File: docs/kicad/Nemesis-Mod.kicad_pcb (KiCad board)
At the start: 2 copper layers, 45.7 x 59.7 mm, 6 parts, among them P1 Pololu_5V_Step_Down_Regulator, SW1 SW1

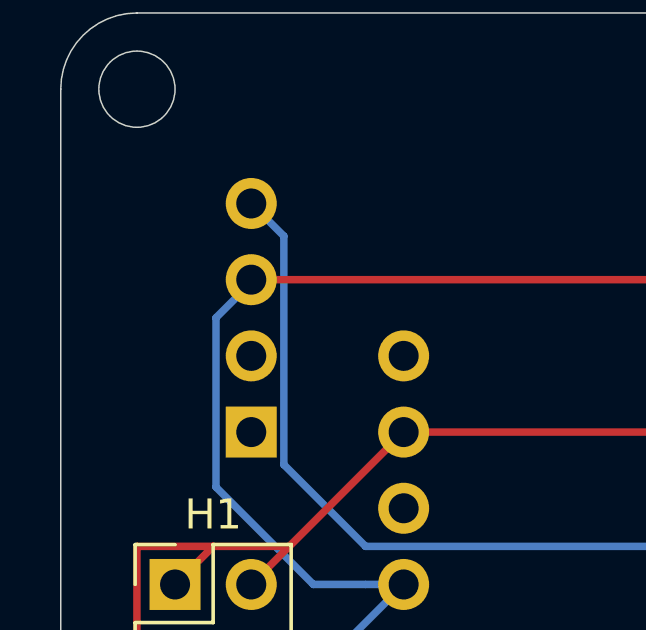
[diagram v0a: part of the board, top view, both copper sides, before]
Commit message: Adding on-board documentation for power.
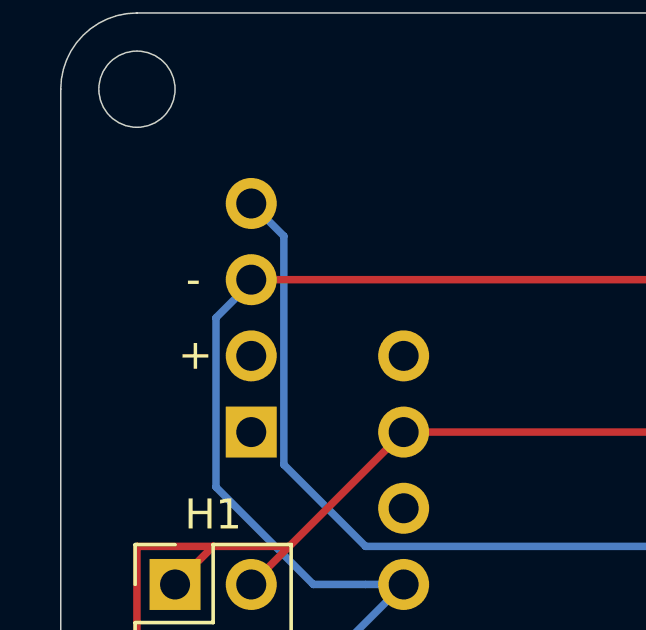
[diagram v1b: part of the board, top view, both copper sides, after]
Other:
- board text added: "+"
- board text added: "-"
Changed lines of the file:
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@@
     (property "Sheetname" "Mainboard")
     (attr through_hole)
-    (fp_text reference "P1" (at 0 -7.62 90) (layer "B.SilkS")
+    (fp_text reference "P1" (at 0 -7.0612 90) (layer "B.SilkS")
       (effects (font (size 1 1) (thickness 0.15)) (justify mirror))
     )
@@
   (gr_circle (center 132.08 80.01) (end 133.35 80.01) (layer "Edge.Cuts") (width 0.05) (fill none))
   (gr_line (start 134.62 80.01) (end 134.62 129.54) (layer "Edge.Cuts") (width 0.05))
+  (gr_text "-" (at 93.3196 86.36) (layer "F.SilkS")
+    (effects (font (size 1 1) (thickness 0.15)))
+  )
+  (gr_text "+" (at 93.4212 88.9 270) (layer "F.SilkS")
+    (effects (font (size 1 1) (thickness 0.15)))
+  )
   (segment (start 123.77 86.36) (end 125.73 88.32) (width 0.25) (layer "F.Cu") (net 2))
   (segment (start 95.25 86.36) (end 123.77 86.36) (width 0.25) (layer "F.Cu") (net 2))

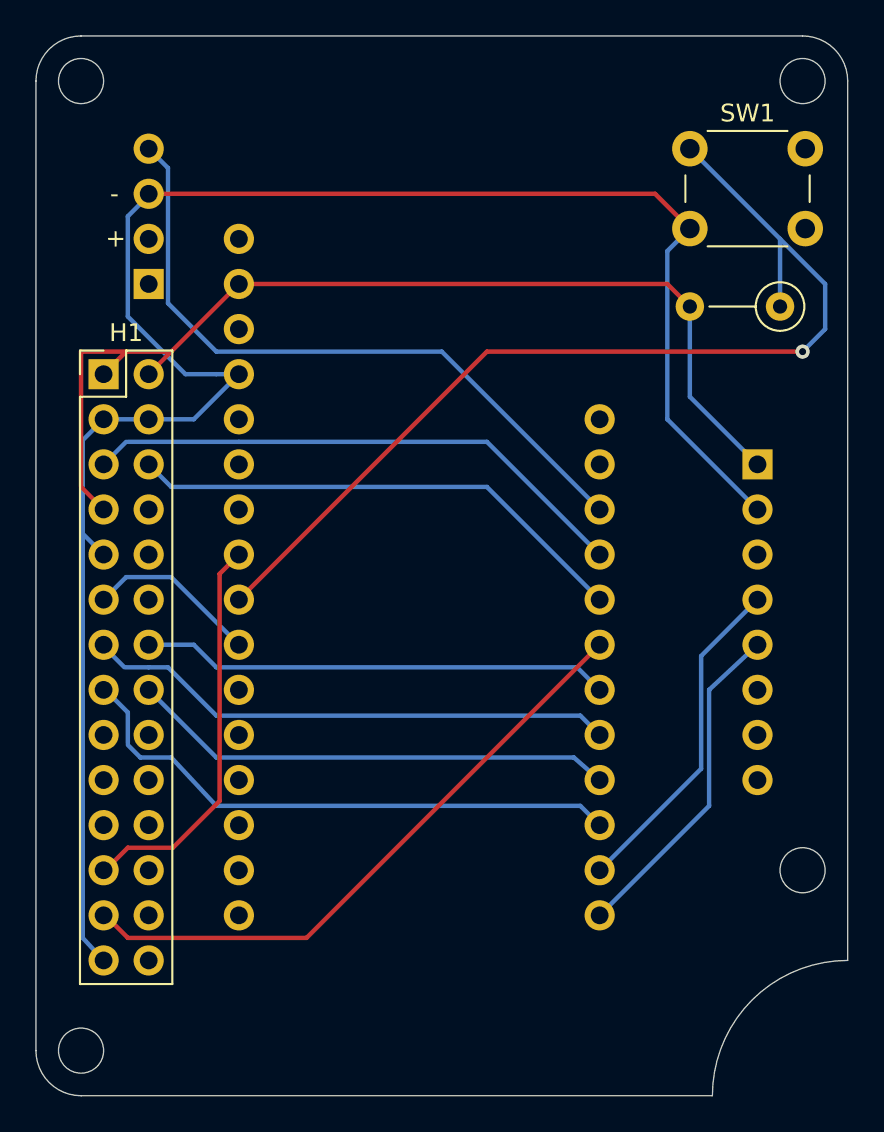
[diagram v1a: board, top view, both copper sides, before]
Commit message: Updating design to use SD card.
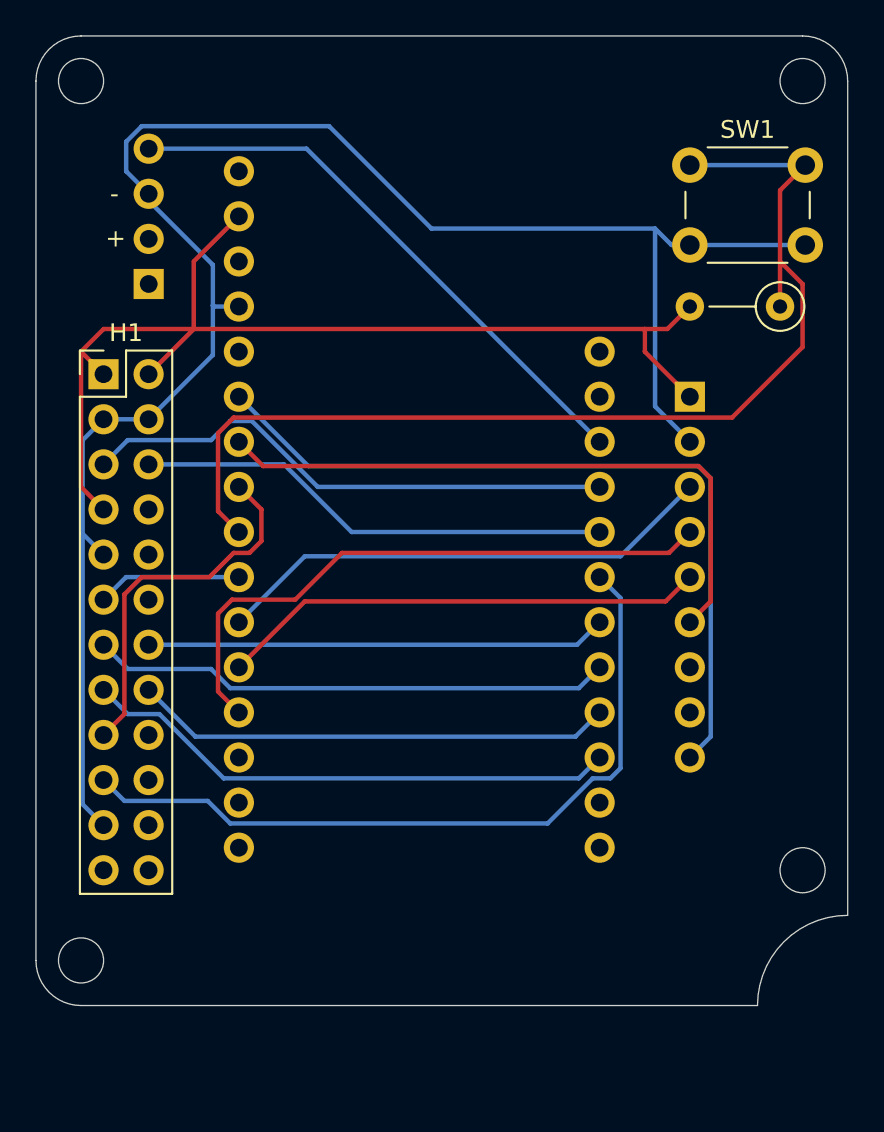
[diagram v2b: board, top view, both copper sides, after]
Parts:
- removed F1: FRAM Breakout, Adafruit:Adafruit_I2C_FRAM_Breakout
- added U1: Adafruit_MicroSD_SPI_Breakout, Adafruit:Adafruit_MicroSD_Breakout, B.Cu at (116.8, 108.7)
- H1: footprint Connector_PinHeader_2.54mm:PinHeader_2x14_P2.54mm_Vertical -> Connector_PinHeader_2.54mm:PinHeader_2x12_P2.54mm_Vertical
- moved MCU1 3.81 mm to (110.5, 104.1)
- moved SW1 0.93 mm to (125.7, 84.7)
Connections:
- net /Hopper Lock/SOFT_LOCK1 renamed /Mainboard/SOFT_LOCK1
- H1 pad 17: unconnected-(H1-Pad17) -> /Mainboard/M3SLP
- H1 pad 19: unconnected-(H1-Pad19) -> /Mainboard/M3PWM
- H1 pad 21: unconnected-(H1-Pad21) -> GND
- H1 pad 23: /Mainboard/M3SLP -> unconnected-(H1-Pad23)
- MCU1 pad 11: unconnected-(MCU1-Pad11) -> /Mainboard/SPI_CLK
- MCU1 pad 12: unconnected-(MCU1-Pad12) -> /Mainboard/SPI_M_OUT
- MCU1 pad 13: unconnected-(MCU1-Pad13) -> /Mainboard/SPI_M_IN
- MCU1 pad 6: unconnected-(MCU1-Pad6) -> /Mainboard/SD_DETECT
- MCU1 pad 7: unconnected-(MCU1-Pad7) -> /Mainboard/SD_SELECT
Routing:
- net /Mainboard/SD_DETECT: track 0.00 -> 44.7 mm
- net /Mainboard/SD_SELECT: track 0.00 -> 36.0 mm
- net /Mainboard/SPI_M_IN: track 0.00 -> 34.5 mm
- net /Mainboard/SPI_CLK: track 0.00 -> 28.6 mm
- net /Mainboard/SPI_M_OUT: track 0.00 -> 27.5 mm
- net /Mainboard/SDA: track 19.0 -> 0.00 mm
- net /Mainboard/SCL: track 18.9 -> 0.00 mm
- net /Mainboard/M3PWM: track 35.3 -> 42.7 mm
- net +5V: track 38.3 -> 32.2 mm
- net /Mainboard/RESET_DOWN: track 56.5 -> 61.4 mm, vias 1 -> 0
- net GND: track 106.3 -> 102.9 mm
- net +3V3: track 59.9 -> 62.4 mm
- net /Mainboard/M1PWM: track 32.2 -> 30.5 mm
- net /Mainboard/M3SLP: track 22.5 -> 20.9 mm
- net /Mainboard/SOFT_LOCK1: track 9.72 -> 8.15 mm
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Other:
- board size 45.7 x 59.7 mm -> 45.7 x 54.6 mm
